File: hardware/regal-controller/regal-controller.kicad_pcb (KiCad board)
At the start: 2 copper layers, 56.5 x 65 mm, 23 parts, among them J1 Raspberry_Pi_2_3, J2 Barrel_Jack_Switch_Pin3Ring, J3 Conn_02x05_Odd_Even, J4 Conn_01x02_Male, J5 Conn_01x02_Male, U1 SN65HVD230, U2 MCP2515, Y1 8MHz

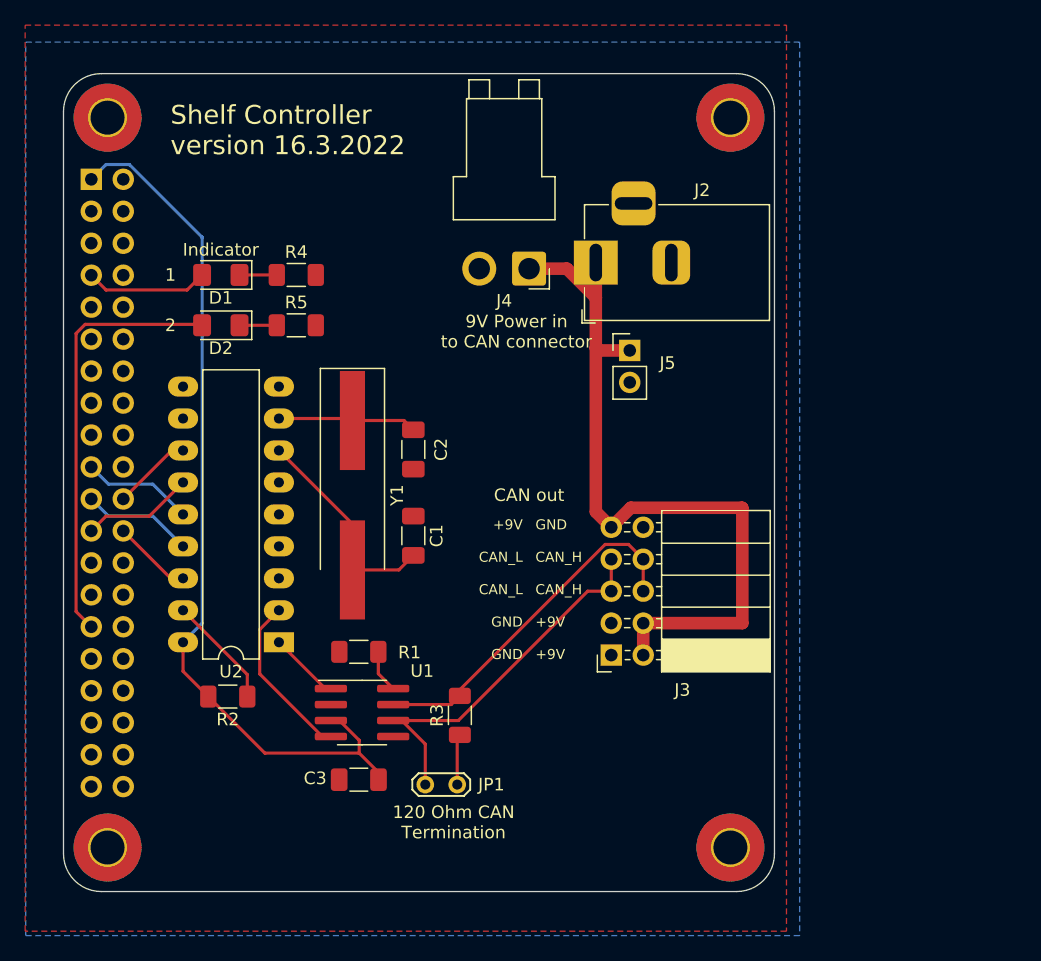
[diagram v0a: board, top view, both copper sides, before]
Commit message: 40pol connector rotated and other small mods.
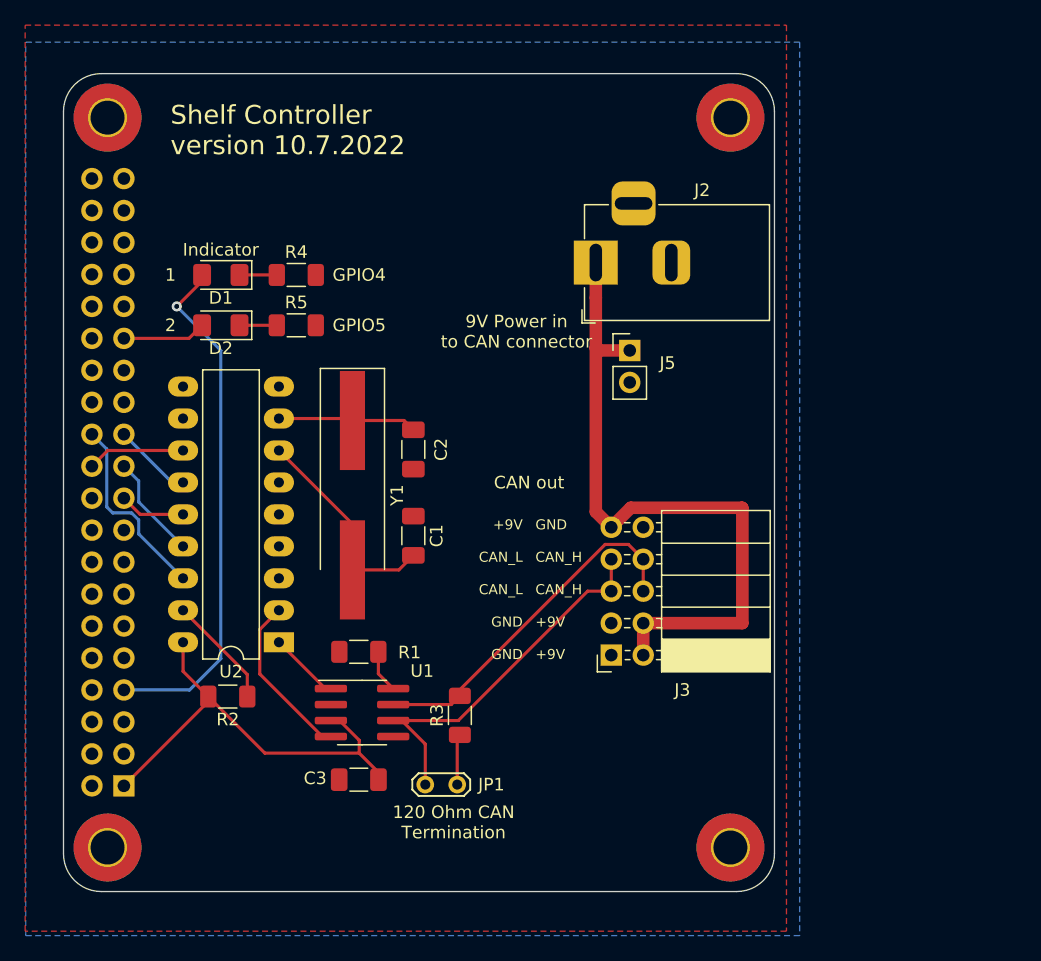
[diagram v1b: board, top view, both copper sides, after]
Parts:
- removed J4: Conn_01x02_Male, Connector_JST:JST_VH_B2PS-VH_1x02_P3.96mm_Horizontal
- moved J1 48.3 mm to (84.3, 107.1), turned to 0 degrees
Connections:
- J2 pad 2: unconnected-(J2-Pad2) -> GND
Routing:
- net +3V3: track 70.2 -> 35.5 mm
- net Net-(D1-Pad2): track 9.78 -> 41.5 mm, vias 0 -> 1
- net Net-(D2-Pad2): track 34.2 -> 6.64 mm
- net /CAN_CS: track 7.36 -> 15.3 mm
- net +9V: track 61.2 -> 54.9 mm
- net /MOSI: track 8.85 -> 5.23 mm
- net /SPI_CLK: track 8.89 -> 6.29 mm
- net /CAN_INT: track 6.35 -> 7.76 mm
- net /MISO: track 8.85 -> 8.31 mm
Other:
- board text added: "GPIO4"
- board text added: "GPIO5"
- board text added: "Shelf Controller version 10.7.2022"
- board text removed: "Shelf Controller version 16.3.2022"

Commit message: shelf controller USB added
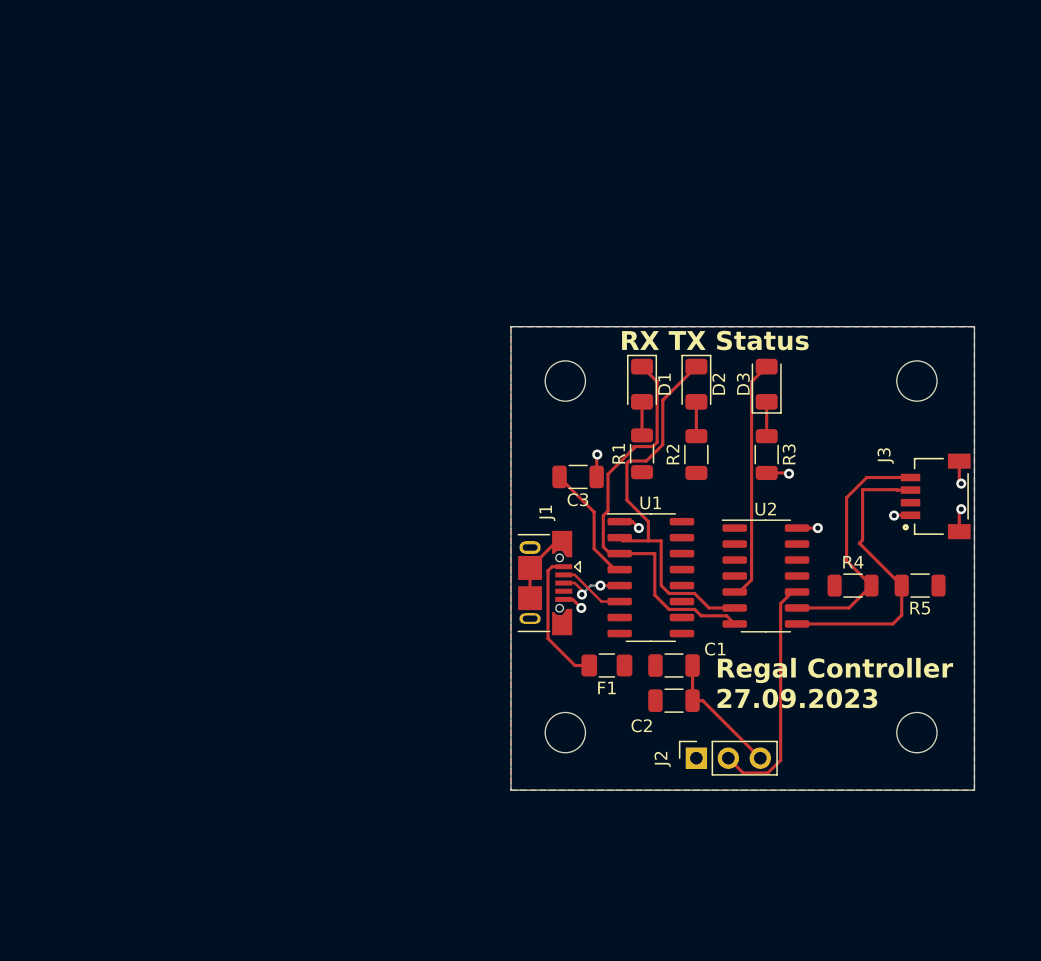
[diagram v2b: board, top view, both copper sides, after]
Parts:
- removed J5: Conn_01x02_Male, Connector_PinHeader_2.54mm:PinHeader_1x02_P2.54mm_Vertical
- removed JP1: Jumper_2_Open, TestPoint:TestPoint_2Pads_Pitch2.54mm_Drill0.8mm
- removed Y1: 8MHz, Crystal:Crystal_SMD_HC49-SD_HandSoldering
- added D3: LED, LED_SMD:LED_1206_3216Metric, F.Cu at (135.4, 75.2)
- added F1: Polyfuse 500mA, Fuse:Fuse_1206_3216Metric, F.Cu at (122.7, 97.5)
- C1: value 22pF -> 0.1u; footprint Capacitor_SMD:C_1206_3216Metric_Pad1.33x1.80mm_HandSolder -> Capacitor_SMD:C_1206_3216Metric
- C2: value 22pF -> 10u; footprint Capacitor_SMD:C_1206_3216Metric_Pad1.33x1.80mm_HandSolder -> Capacitor_SMD:C_1206_3216Metric
- C3: value 100n -> 10n; footprint Capacitor_SMD:C_1206_3216Metric_Pad1.33x1.80mm_HandSolder -> Capacitor_SMD:C_1206_3216Metric
- D1, D2: footprint LED_SMD:LED_1206_3216Metric_Pad1.42x1.75mm_HandSolder -> LED_SMD:LED_1206_3216Metric
- H1, H2, H3, H4: value MountingHole_Pad -> MountingHole; footprint MountingHole:MountingHole_2.7mm_M2.5_Pad_TopBottom -> MountingHole:MountingHole_3.2mm_M3
- J1: value Raspberry_Pi_2_3 -> USB_B_Micro; footprint Connector_PinSocket_2.54mm:PinSocket_2x20_P2.54mm_Vertical -> Connector_USB:USB_Micro-B_XKB_U254-051T-4BH83-F1S; moved to F.Cu
- J2: value Barrel_Jack_Switch_Pin3Ring -> Conn_01x03; footprint Connector_BarrelJack:BarrelJack_Horizontal -> Connector_PinSocket_2.54mm:PinSocket_1x03_P2.54mm_Vertical
- J3: value Conn_02x05_Odd_Even -> SM04B-SRSS-TB(LF)(SN); footprint Connector_PinSocket_2.54mm:PinSocket_2x05_P2.54mm_Horizontal -> MyConnector:JST_SM04B-SRSS-TB(LF)(SN)
- R1: footprint Resistor_SMD:R_1206_3216Metric_Pad1.30x1.75mm_HandSolder -> Resistor_SMD:R_1206_3216Metric
- R2: value 10k -> 1k; footprint Resistor_SMD:R_1206_3216Metric_Pad1.30x1.75mm_HandSolder -> Resistor_SMD:R_1206_3216Metric
- R3: value 120 -> 1k; footprint Resistor_SMD:R_1206_3216Metric_Pad1.30x1.75mm_HandSolder -> Resistor_SMD:R_1206_3216Metric
- R4, R5: value 120 -> 2.2k; footprint Resistor_SMD:R_1206_3216Metric_Pad1.30x1.75mm_HandSolder -> Resistor_SMD:R_1206_3216Metric
- U1: value SN65HVD230 -> CH340C; footprint Package_SO:SOIC-8_3.9x4.9mm_P1.27mm -> Package_SO:SOIC-16_3.9x9.9mm_P1.27mm
- U2: value MCP2515 -> ATtiny1614-SS; footprint Package_DIP:DIP-18_W7.62mm_LongPads -> Package_SO:SOIC-14_3.9x8.7mm_P1.27mm
- moved H4 65.0 mm to (147.3, 102.9)
- moved R5 53.7 mm to (147.6, 91.2), turned to 180 degrees
- moved R4 50.7 mm to (142.2, 91.2)
- moved H1 42.0 mm to (119.4, 74.9)
- moved R2 41.9 mm to (129.8, 80.8), turned to 90 degrees
- moved J2 40.2 mm to (129.8, 104.9), turned to 90 degrees
- moved U2 39.1 mm to (135.3, 90.4), turned to 0 degrees
- moved D2 38.1 mm to (129.8, 75.2), turned to -90 degrees
- moved J1 36.4 mm to (117.0, 91.0), turned to -90 degrees
- moved D1 34.6 mm to (125.5, 75.2), turned to -90 degrees
- moved R3 32.0 mm to (135.4, 80.8), turned to -90 degrees
- moved C3 29.7 mm to (120.4, 82.5), turned to 180 degrees
- moved C2 28.8 mm to (128.0, 100.3), turned to 0 degrees
- moved R1 27.5 mm to (125.5, 80.7), turned to 90 degrees
- moved J3 26.9 mm to (146.8, 84.1), turned to 90 degrees
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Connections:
- C1 pad 1: GND -> +5V
- C1 pad 2: Net-(C1-Pad2) -> GND
- C2 pad 1: GND -> +5V
- C2 pad 2: Net-(C2-Pad2) -> GND
- C3 pad 2: +3V3 -> Net-(U1-V3)
- D1 pad 1: Net-(D1-Pad1) -> Net-(D1-K)
- D1 pad 2: Net-(D1-Pad2) -> Net-(D1-A)
- D2 pad 1: Net-(D2-Pad1) -> Net-(D2-K)
- D2 pad 2: Net-(D2-Pad2) -> Net-(D2-A)
- J1 pad 1: +3V3 -> /VBUS
- J1 pad 2: unconnected-(J1-Pad2) -> /USB D-
- J1 pad 3: unconnected-(J1-Pad3) -> /USB D+
- J1 pad 5: unconnected-(J1-Pad5) -> GND
- J1 pad 6: GND -> unconnected-(J1-Shield-Pad6)
- J2 pad 1: +9V -> +5V
- J2 pad 2: GND -> Net-(J2-Pin_2)
- J3 pad 2: +9V -> +5V
- J3 pad 3: GND -> SDA
- J3 pad 4: +9V -> SCL
- R1 pad 1: Net-(R1-Pad1) -> +5V
- R1 pad 2: GND -> Net-(D1-A)
- R2 pad 1: Net-(R2-Pad1) -> +5V
- R2 pad 2: +3V3 -> Net-(D2-A)
- R3 pad 2: /CAN_H -> GND
- R4 pad 1: Net-(D1-Pad1) -> +5V
- R4 pad 2: GND -> SCL
- R5 pad 1: Net-(D2-Pad1) -> +5V
- R5 pad 2: GND -> SDA
- U1 pad 1: Net-(U1-Pad1) -> GND
- U1 pad 2: GND -> Net-(D2-K)
- U1 pad 3: +3V3 -> Net-(D1-K)
- U1 pad 4: Net-(U1-Pad4) -> Net-(U1-V3)
- U1 pad 5: unconnected-(U1-Pad5) -> /USB D+
- U1 pad 6: /CAN_L -> /USB D-
- U1 pad 7: /CAN_H -> unconnected-(U1-NC-Pad7)
- U1 pad 8: Net-(R1-Pad1) -> unconnected-(U1-NC-Pad8)
- U2 pad 1: Net-(U1-Pad1) -> +5V
- U2 pad 10: unconnected-(U2-Pad10) -> Net-(J2-Pin_2)
- U2 pad 12: /CAN_INT -> unconnected-(U2-PA2-Pad12)
- U2 pad 13: /SPI_CLK -> unconnected-(U2-PA3-Pad13)
- U2 pad 14: /MOSI -> GND
- U2 pad 2: Net-(U1-Pad4) -> unconnected-(U2-PA4-Pad2)
- U2 pad 5: unconnected-(U2-Pad5) -> Net-(D3-A)
- U2 pad 6: unconnected-(U2-Pad6) -> Net-(D2-K)
- U2 pad 7: Net-(C1-Pad2) -> Net-(D1-K)
- U2 pad 8: Net-(C2-Pad2) -> SDA
- U2 pad 9: GND -> SCL
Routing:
- net +9V: track 54.9 -> 0.00 mm
- net Net-(D1-Pad2): track 41.5 -> 0.00 mm, vias 1 -> 0
- net +3V3: track 35.5 -> 0.00 mm
- net Net-(D1-K): track 0.00 -> 32.4 mm
- net Net-(D2-K): track 0.00 -> 31.2 mm
- net /CAN_L: track 30.7 -> 0.00 mm
- net /CAN_H: track 28.5 -> 0.00 mm
- net SDA: track 0.00 -> 23.9 mm
- net GND: track 0.00 -> 23.3 mm, vias 0 -> 8
- net SCL: track 0.00 -> 20.2 mm
- net Net-(J2-Pin_2): track 0.00 -> 19.2 mm
- net Net-(D3-A): track 0.00 -> 19.2 mm
- net Net-(C1-Pad2): track 17.2 -> 0.00 mm
- net /CAN_CS: track 15.3 -> 0.00 mm
- net Net-(U1-Pad4): track 13.4 -> 0.00 mm
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- added copper zone on F.Cu, net +5V
- removed copper zone on F.Cu, net GND
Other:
- board size 56.5 x 65 mm -> 36.8 x 36.8 mm
- board text added: "RX TX Status"
- board text added: "Regal Controller 27.09.2023"
- board text removed: "+9V CAN_L CAN_L GND GND"
- board text removed: "1"
- board text removed: "120 Ohm CAN Termination"
- board text removed: "2"
- board text removed: "9V Power in to CAN connector"
- board text removed: "CAN out"
- board text removed: "GND CAN_H CAN_H +9V +9V"
- board text removed: "GPIO4"
- board text removed: "GPIO5"
- board text removed: "Indicator"
- board text removed: "Shelf Controller version 10.7.2022"
